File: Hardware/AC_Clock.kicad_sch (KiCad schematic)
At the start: 44 parts, among them J1 L, J2 N, SW1 Min_PB, SW2 Hr_PB, T1 10:1, U1 AZ1117-5.0, U2 LTV-817S, U3 4040, U4 74LS393, U5 74LS393

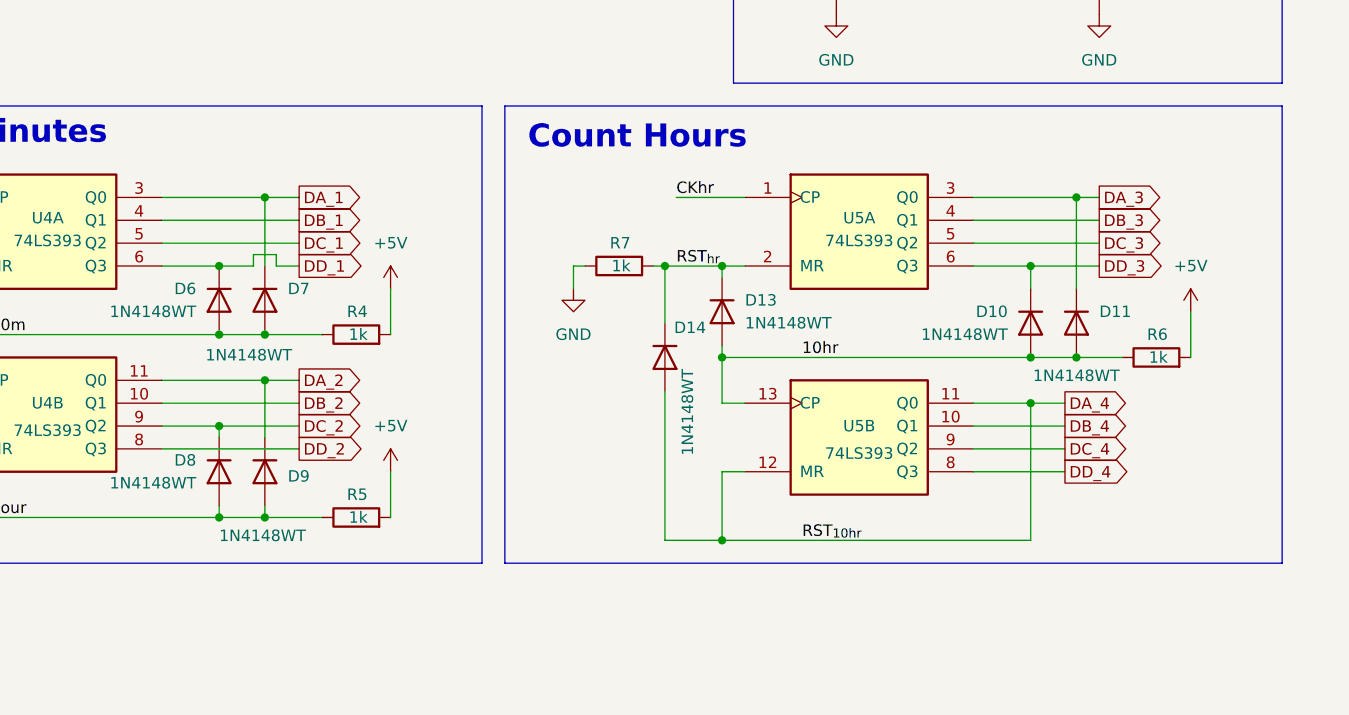
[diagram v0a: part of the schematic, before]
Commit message: Fix the counters' reset signals
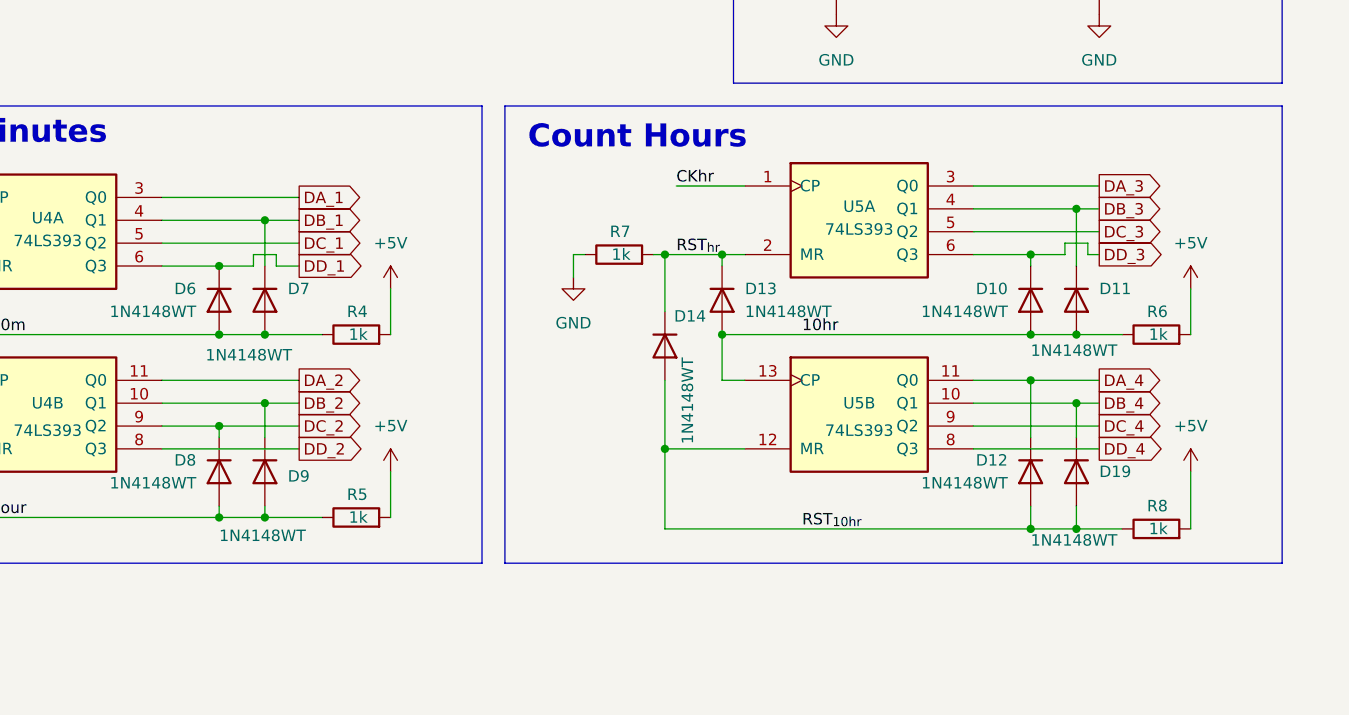
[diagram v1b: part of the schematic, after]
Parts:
- added D12, D19: 1N4148WT, Diode_SMD:D_SOD-523, symbol Diode:1N4148WT
- added R8: 1k, Resistor_SMD:R_0603_1608Metric, symbol Device:R
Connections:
- net +5V: now also R8.2
- net DA_1: no longer D7.1 (K)
- net DA_2: no longer D9.1 (K)
- net DA_3: no longer D11.1 (K)
- net DA_4: now also D12.1 (K); no longer D14.2 (A), U5.12 (MR)
- net DB_1: now also D7.1 (K)
- net DB_2: now also D9.1 (K)
- net DB_3: now also D11.1 (K)
- net DB_4: now also D19.1 (K)
- new net RST_{10hr}: D12.2 (A), D14.2 (A), D19.2 (A), R8.1, U5.12 (MR)
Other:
- moved on the sheet: D10, D11, D13, D14, R6, R7, U5A, U5B

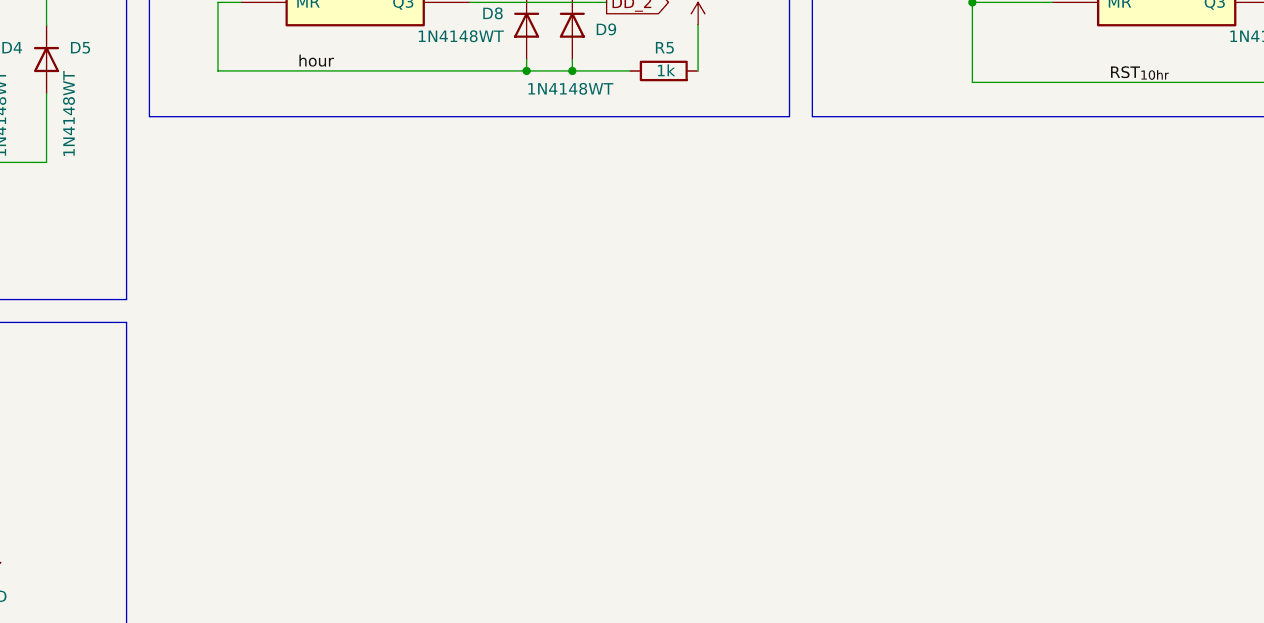
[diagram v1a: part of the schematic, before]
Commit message: Add in connectors for display board interconnect
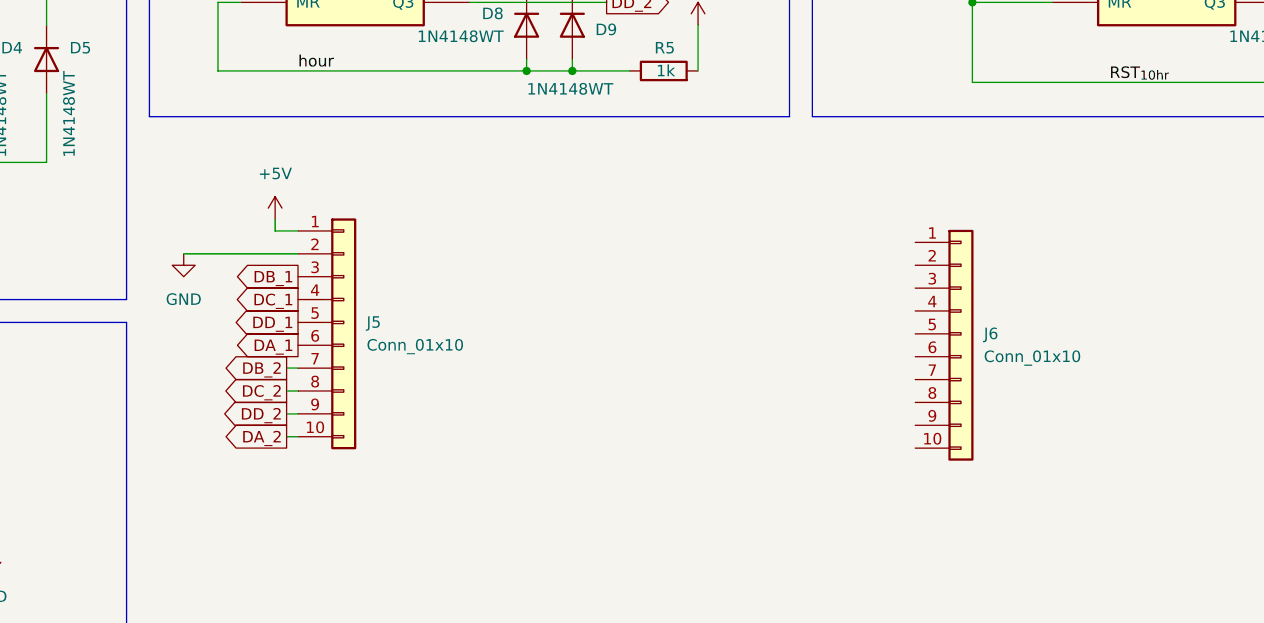
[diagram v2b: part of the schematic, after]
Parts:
- added J5, J6: Conn_01x10, Connector_PinHeader_2.54mm:PinHeader_1x10_P2.54mm_Vertical, symbol Connector_Generic:Conn_01x10
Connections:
- net +5V: now also J5.1 (Pin_1)
- net DA_1: now also J5.6 (Pin_6)
- net DA_2: now also J5.10 (Pin_10)
- net DB_1: now also J5.3 (Pin_3)
- net DB_2: now also J5.7 (Pin_7)
- net DC_1: now also J5.4 (Pin_4)
- net DC_2: now also J5.8 (Pin_8)
- net DD_1: now also J5.5 (Pin_5)
- net DD_2: now also J5.9 (Pin_9)
- net GND: now also J5.2 (Pin_2)

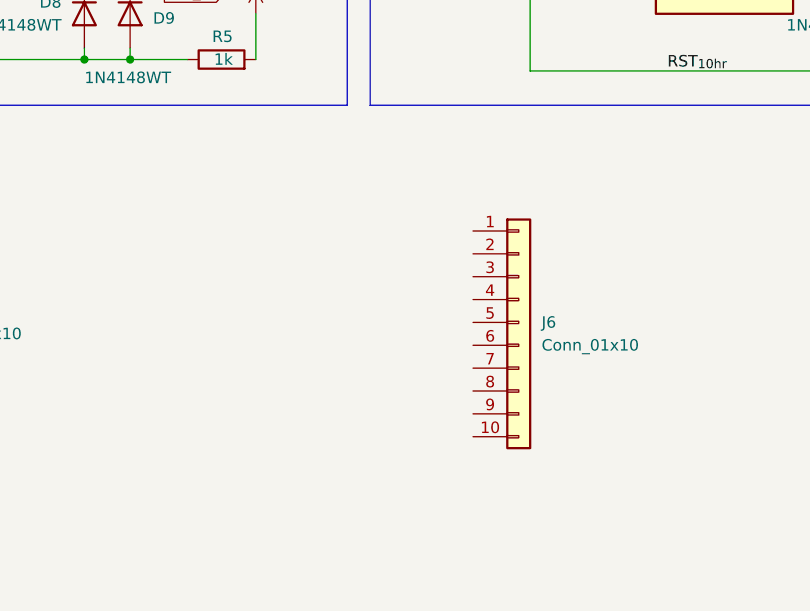
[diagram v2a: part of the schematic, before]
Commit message: Wire up the Hours connectors
Signed-off-by: Joel Cranmer <42.joel.cranmer@gmail.com>
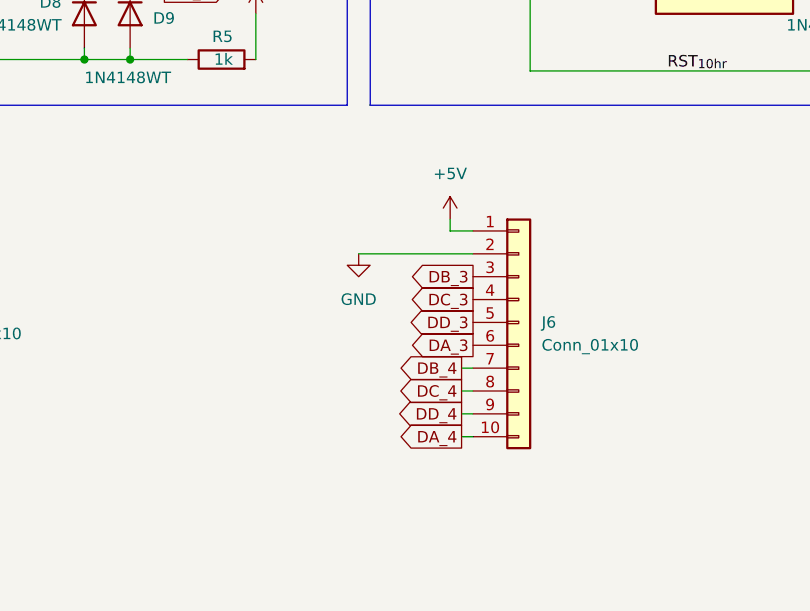
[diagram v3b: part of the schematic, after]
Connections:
- net +5V: now also J6.1 (Pin_1)
- net DA_3: now also J6.6 (Pin_6)
- net DA_4: now also J6.10 (Pin_10)
- net DB_3: now also J6.3 (Pin_3)
- net DB_4: now also J6.7 (Pin_7)
- net DC_3: now also J6.4 (Pin_4)
- net DC_4: now also J6.8 (Pin_8)
- net DD_3: now also J6.5 (Pin_5)
- net DD_4: now also J6.9 (Pin_9)
- net GND: now also J6.2 (Pin_2)

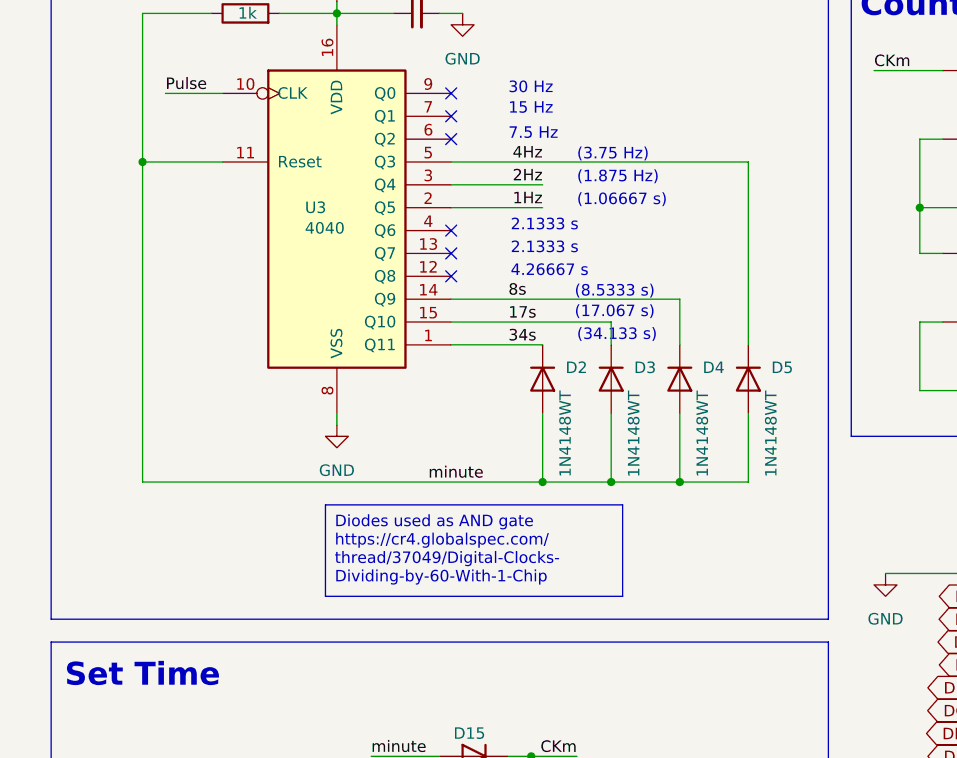
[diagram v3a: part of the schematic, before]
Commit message: Fix 12-bit counter overflow
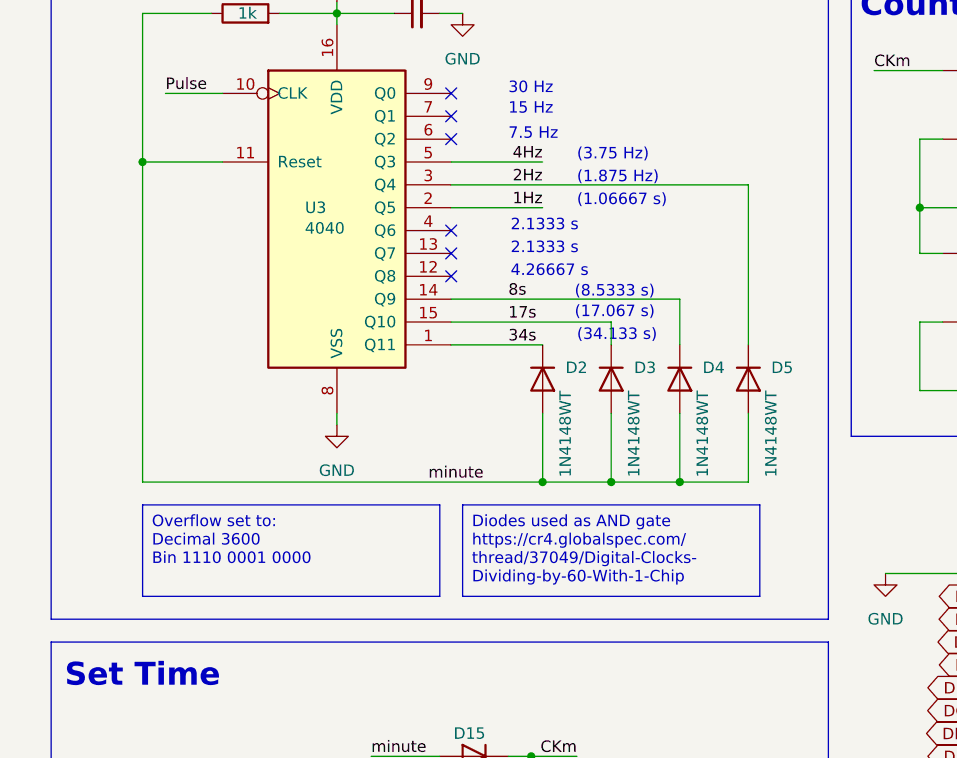
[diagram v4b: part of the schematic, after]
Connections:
- net 2Hz: now also D5.1 (K)
- net 4Hz: no longer D5.1 (K)
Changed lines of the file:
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@@
 	(wire
 		(pts
+			(xy 59.69 81.28) (xy 69.85 81.28)
+		)
+		(stroke
+			(width 0)
+			(type default)
+		)
+	)
+	(wire
+		(pts
 			(xy 229.87 99.06) (xy 243.84 99.06)
 		)
@@
 	(wire
 		(pts
-			(xy 59.69 83.82) (xy 69.85 83.82)
+			(xy 59.69 83.82) (xy 92.71 83.82)
 		)
 		(stroke
@@
 	(wire
 		(pts
-			(xy 59.69 81.28) (xy 92.71 81.28)
-		)
-		(stroke
-			(width 0)
-			(type default)
-		)
-	)
-	(wire
-		(pts
 			(xy 146.05 96.52) (xy 146.05 97.79)
 		)
@@
 	(wire
 		(pts
+			(xy 92.71 83.82) (xy 92.71 101.6)
+		)
+		(stroke
+			(width 0)
+			(type default)
+		)
+	)
+	(wire
+		(pts
 			(xy 254 101.6) (xy 254 107.95)
 		)
@@
 	(wire
 		(pts
-			(xy 92.71 101.6) (xy 92.71 81.28)
-		)
-		(stroke
-			(width 0)
-			(type default)
-		)
-	)
-	(wire
-		(pts
 			(xy 119.38 142.24) (xy 120.65 142.24)
 		)
@@
 	(text_box "Diodes used as AND gate\nhttps://cr4.globalspec.com/\nthread/37049/Digital-Clocks-\nDividing-by-60-With-1-Chip"
 		(exclude_from_sim no)
-		(at 45.72 119.38 0)
+		(at 60.96 119.38 0)
+		(size 33.02 10.16)
+		(stroke
+			(width 0)
+			(type default)
+		)
+		(fill
+			(type none)
+		)
+		(effects
+			(font
+				(size 1.27 1.27)
+			)
+			(justify left top)
+		)
+	)
+	(text_box "Overflow set to:\nDecimal 3600\nBin 1110 0001 0000"
+		(exclude_from_sim no)
+		(at 25.4 119.38 0)
 		(size 33.02 10.16)
 		(stroke
@@
 		(pin "12"
 		)
+		(pin "10"
+		)
+		(pin "9"
+		)
 		(instances
